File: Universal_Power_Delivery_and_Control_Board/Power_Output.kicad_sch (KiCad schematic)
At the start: 40 parts, among them CN1 B03B-XASK-1-A(LF)(SN), CN2 B03B-XASK-1-A(LF)(SN), CN3 B03B-XASK-1-A(LF)(SN), CN4 B03B-XASK-1-A(LF)(SN), U10 SN74LVC1G17DCKR, U11 SN74LVC1G17DCKR, U12 SN74LVC1G17DCKR, U13 SN74LVC1G17DCKR, U14 SN74LVC1G17DCKR, U8 TPS51385RJNR, U9 TPS24751RUVR

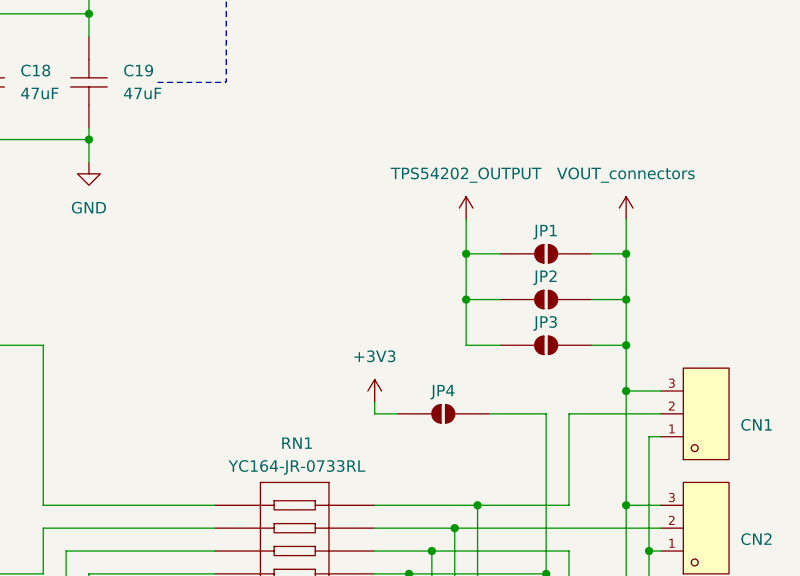
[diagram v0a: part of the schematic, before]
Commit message: Switched to a 4 layer stackup and routed the digital output section.
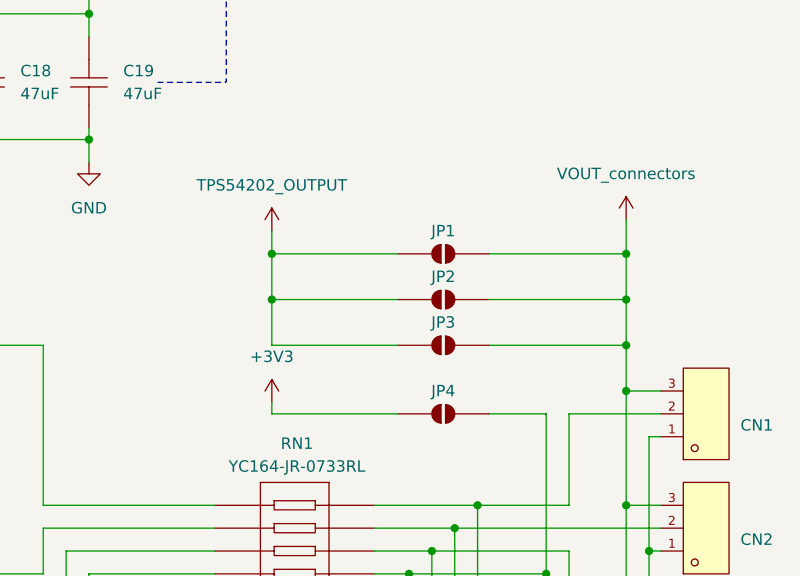
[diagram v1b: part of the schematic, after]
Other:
- moved on the sheet: JP1, JP2, JP3
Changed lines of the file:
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@@
 	)
 	(junction
-		(at 227.33 69.85)
-		(diameter 0)
-		(color 0 0 0 0)
-	)
-	(junction
 		(at 247.65 142.24)
 		(diameter 0)
@@
 	)
 	(junction
+		(at 245.11 64.77)
+		(diameter 0)
+		(color 0 0 0 0)
+	)
+	(junction
+		(at 245.11 69.85)
+		(diameter 0)
+		(color 0 0 0 0)
+	)
+	(junction
 		(at 245.11 80.01)
 		(diameter 0)
@@
 	)
 	(junction
-		(at 227.33 64.77)
-		(diameter 0)
-		(color 0 0 0 0)
-	)
-	(junction
 		(at 223.52 97.79)
 		(diameter 0)
@@
 	)
 	(junction
+		(at 205.74 69.85)
+		(diameter 0)
+		(color 0 0 0 0)
+	)
+	(junction
 		(at 137.16 38.1)
 		(diameter 0)
@@
 	)
 	(junction
-		(at 245.11 64.77)
+		(at 205.74 64.77)
 		(diameter 0)
 		(color 0 0 0 0)
@@
 	)
 	(junction
-		(at 245.11 69.85)
-		(diameter 0)
-		(color 0 0 0 0)
-	)
-	(junction
 		(at 146.05 176.53)
 		(diameter 0)
@@
 	(wire
 		(pts
-			(xy 217.17 81.28) (xy 217.17 82.55)
+			(xy 205.74 81.28) (xy 205.74 82.55)
 		)
 		(stroke
@@
 	(wire
 		(pts
-			(xy 227.33 60.96) (xy 227.33 64.77)
+			(xy 205.74 62.23) (xy 205.74 64.77)
 		)
 		(stroke
@@
 	(wire
 		(pts
-			(xy 227.33 69.85) (xy 227.33 74.93)
+			(xy 205.74 69.85) (xy 205.74 74.93)
 		)
 		(stroke
@@
 	(wire
 		(pts
+			(xy 205.74 69.85) (xy 219.71 69.85)
+		)
+		(stroke
+			(width 0)
+			(type default)
+		)
+	)
+	(wire
+		(pts
 			(xy 78.74 104.14) (xy 97.79 104.14)
 		)
@@
 	(wire
 		(pts
-			(xy 245.11 64.77) (xy 245.11 74.93)
+			(xy 245.11 64.77) (xy 245.11 69.85)
 		)
 		(stroke
@@
 	(wire
 		(pts
-			(xy 227.33 64.77) (xy 231.14 64.77)
-		)
-		(stroke
-			(width 0)
-			(type default)
-		)
-	)
-	(wire
-		(pts
 			(xy 76.2 156.21) (xy 76.2 158.75)
 		)
@@
 	(wire
 		(pts
-			(xy 227.33 64.77) (xy 227.33 69.85)
+			(xy 205.74 64.77) (xy 205.74 69.85)
 		)
 		(stroke
@@
 	(wire
 		(pts
-			(xy 241.3 74.93) (xy 245.11 74.93)
+			(xy 229.87 74.93) (xy 245.11 74.93)
 		)
 		(stroke
@@
 	(wire
 		(pts
-			(xy 217.17 82.55) (xy 219.71 82.55)
+			(xy 205.74 82.55) (xy 219.71 82.55)
 		)
 		(stroke
@@
 	(wire
 		(pts
-			(xy 241.3 64.77) (xy 245.11 64.77)
+			(xy 229.87 64.77) (xy 245.11 64.77)
 		)
 		(stroke
@@
 	(wire
 		(pts
+			(xy 205.74 64.77) (xy 219.71 64.77)
+		)
+		(stroke
+			(width 0)
+			(type default)
+		)
+	)
+	(wire
+		(pts
 			(xy 247.65 123.19) (xy 248.92 123.19)
 		)
@@
 	(wire
 		(pts
-			(xy 241.3 69.85) (xy 245.11 69.85)
+			(xy 229.87 69.85) (xy 245.11 69.85)
 		)
 		(stroke
@@
 	(wire
 		(pts
-			(xy 227.33 69.85) (xy 231.14 69.85)
-		)
-		(stroke
-			(width 0)
-			(type default)
-		)
-	)
-	(wire
-		(pts
 			(xy 146.05 144.78) (xy 146.05 151.13)
 		)
@@
 	(wire
 		(pts
-			(xy 227.33 74.93) (xy 231.14 74.93)
+			(xy 205.74 74.93) (xy 219.71 74.93)
 		)
 		(stroke
@@
 	(wire
 		(pts
+			(xy 245.11 69.85) (xy 245.11 74.93)
+		)
+		(stroke
+			(width 0)
+			(type default)
+		)
+	)
+	(wire
+		(pts
 			(xy 116.84 140.97) (xy 116.84 138.43)
 		)
@@
 	(symbol
 		(lib_id "power:+1V0")
-		(at 217.17 81.28 0)
+		(at 205.74 81.28 0)
 		(unit 1)
 		(body_style 1)
@@
 		(fields_autoplaced yes)
 		(property "Reference" "#PWR043"
-			(at 217.17 85.09 0)
+			(at 205.74 85.09 0)
 			(hide yes)
 			(show_name no)
@@
 		)
 		(property "Value" "+3V3"
-			(at 217.17 76.2 0)
+			(at 205.74 76.2 0)
 			(show_name no)
 			(do_not_autoplace no)
@@
 		)
 		(property "Footprint" ""
-			(at 217.17 81.28 0)
+			(at 205.74 81.28 0)
 			(hide yes)
 			(show_name no)
@@
 		)
 		(property "Datasheet" ""
-			(at 217.17 81.28 0)
+			(at 205.74 81.28 0)
 			(hide yes)
 			(show_name no)
@@
 		)
 		(property "Description" "Power symbol creates a global label with name \"+1V0\""
-			(at 217.17 81.28 0)
+			(at 205.74 81.28 0)
 			(hide yes)
 			(show_name no)
@@
 	(symbol
 		(lib_id "Jumper:SolderJumper_2_Open")
-		(at 236.22 69.85 0)
+		(at 224.79 69.85 0)
 		(unit 1)
 		(body_style 1)
@@
 		(dnp no)
 		(property "Reference" "JP2"
-			(at 236.22 67.31 0)
+			(at 224.79 67.31 0)
 			(show_name no)
 			(do_not_autoplace no)
@@
 		)
 		(property "Value" "SolderJumper_2_Open"
-			(at 236.22 66.04 0)
+			(at 224.79 66.04 0)
 			(hide yes)
 			(show_name no)
@@
 		)
 		(property "Footprint" "Jumper:SolderJumper-2_P1.3mm_Open_RoundedPad1.0x1.5mm"
-			(at 236.22 69.85 0)
+			(at 224.79 69.85 0)
 			(hide yes)
 			(show_name no)
@@
 		)
 		(property "Datasheet" ""
-			(at 236.22 77.47 0)
+			(at 224.79 77.47 0)
 			(hide yes)
 			(show_name no)
@@
 		)
 		(property "Description" "Solder Jumper, 2-pole, open"
-			(at 236.22 74.93 0)
+			(at 224.79 74.93 0)
 			(hide yes)
 			(show_name no)
@@
 	(symbol
 		(lib_id "Jumper:SolderJumper_2_Open")
-		(at 236.22 64.77 0)
+		(at 224.79 64.77 0)
 		(unit 1)
 		(body_style 1)
@@
 		(dnp no)
 		(property "Reference" "JP1"
-			(at 236.22 62.23 0)
+			(at 224.79 62.23 0)
 			(show_name no)
 			(do_not_autoplace no)
@@
 		)
 		(property "Value" "SolderJumper_2_Open"
-			(at 236.22 60.96 0)
+			(at 224.79 60.96 0)
 			(hide yes)
 			(show_name no)
@@
 		)
 		(property "Footprint" "Jumper:SolderJumper-2_P1.3mm_Open_RoundedPad1.0x1.5mm"
-			(at 236.22 64.77 0)
+			(at 224.79 64.77 0)
 			(hide yes)
 			(show_name no)
@@
 		)
 		(property "Datasheet" ""
-			(at 236.22 72.39 0)
+			(at 224.79 72.39 0)
 			(hide yes)
 			(show_name no)
@@
 		)
 		(property "Description" "Solder Jumper, 2-pole, open"
-			(at 236.22 69.85 0)
+			(at 224.79 69.85 0)
 			(hide yes)
 			(show_name no)
@@
 	(symbol
 		(lib_id "power:+1V0")
-		(at 227.33 60.96 0)
+		(at 205.74 62.23 0)
 		(unit 1)
 		(body_style 1)
@@
 		(fields_autoplaced yes)
 		(property "Reference" "#PWR041"
-			(at 227.33 64.77 0)
+			(at 205.74 66.04 0)
 			(hide yes)
 			(show_name no)
@@
 		)
 		(property "Value" "TPS54202_OUTPUT"
-			(at 227.33 55.88 0)
+			(at 205.74 57.15 0)
 			(show_name no)
 			(do_not_autoplace no)
@@
 		)
 		(property "Footprint" ""
-			(at 227.33 60.96 0)
+			(at 205.74 62.23 0)
 			(hide yes)
 			(show_name no)
@@
 		)
 		(property "Datasheet" ""
-			(at 227.33 60.96 0)
+			(at 205.74 62.23 0)
 			(hide yes)
 			(show_name no)
@@
 		)
 		(property "Description" "Power symbol creates a global label with name \"+1V0\""
-			(at 227.33 60.96 0)
+			(at 205.74 62.23 0)
 			(hide yes)
 			(show_name no)
@@
 	(symbol
 		(lib_id "Jumper:SolderJumper_2_Open")
-		(at 236.22 74.93 0)
+		(at 224.79 74.93 0)
 		(unit 1)
 		(body_style 1)
@@
 		(dnp no)
 		(property "Reference" "JP3"
-			(at 236.22 72.39 0)
+			(at 224.79 72.39 0)
 			(show_name no)
 			(do_not_autoplace no)
@@
 		)
 		(property "Value" "SolderJumper_2_Open"
-			(at 236.22 71.12 0)
+			(at 224.79 71.12 0)
 			(hide yes)
 			(show_name no)
@@
 		)
 		(property "Footprint" "Jumper:SolderJumper-2_P1.3mm_Open_RoundedPad1.0x1.5mm"
-			(at 236.22 74.93 0)
+			(at 224.79 74.93 0)
 			(hide yes)
 			(show_name no)
@@
 		)
 		(property "Datasheet" ""
-			(at 236.22 82.55 0)
+			(at 224.79 82.55 0)
 			(hide yes)
 			(show_name no)
@@
 		)
 		(property "Description" "Solder Jumper, 2-pole, open"
-			(at 236.22 80.01 0)
+			(at 224.79 80.01 0)
 			(hide yes)
 			(show_name no)

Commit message: Practically finshed the digital output layout, added the i2c io expander as im short on ios.
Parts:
- added C41: 10uF, Capacitor_SMD:C_0805_2012Metric_Pad1.18x1.45mm_HandSolder, symbol Device:C
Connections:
- net +5V_VSYS: now also C41.2
- net GND: now also C41.1
- net at CN1.2, RN1.8: now also FPC1.3; no longer FPC1.1
- net at CN4.2, JP4.2 (B), RN1.5: now also FPC1.9; no longer FPC1.7
- net at CN2.2, RN1.7: now also FPC1.5; no longer FPC1.3
- net at CN3.2, RN1.6: now also FPC1.7; no longer FPC1.5
- net at R18.1: now also FPC1.1; no longer FPC1.9
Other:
- moved on the sheet: R18

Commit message: Added some misc stuff layout almost finished.
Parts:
- removed JP3: SolderJumper_2_Open, Jumper:SolderJumper-2_P1.3mm_Open_RoundedPad1.0x1.5mm, symbol Jumper:SolderJumper_2_Open
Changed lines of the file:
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@@
 	)
 	(junction
-		(at 245.11 74.93)
-		(diameter 0)
-		(color 0 0 0 0)
-	)
-	(junction
 		(at 76.2 153.67)
 		(diameter 0)
@@
 	)
 	(junction
-		(at 205.74 69.85)
-		(diameter 0)
-		(color 0 0 0 0)
-	)
-	(junction
 		(at 137.16 38.1)
 		(diameter 0)
@@
 	(wire
 		(pts
-			(xy 245.11 74.93) (xy 245.11 80.01)
+			(xy 245.11 69.85) (xy 245.11 80.01)
 		)
 		(stroke
@@
 	(wire
 		(pts
-			(xy 205.74 69.85) (xy 205.74 74.93)
-		)
-		(stroke
-			(width 0)
-			(type default)
-		)
-	)
-	(wire
-		(pts
 			(xy 96.52 73.66) (xy 91.44 73.66)
 		)
@@
 	(wire
 		(pts
-			(xy 229.87 74.93) (xy 245.11 74.93)
-		)
-		(stroke
-			(width 0)
-			(type default)
-		)
-	)
-	(wire
-		(pts
 			(xy 223.52 149.86) (xy 248.92 149.86)
 		)
@@
 	(wire
 		(pts
-			(xy 205.74 74.93) (xy 219.71 74.93)
-		)
-		(stroke
-			(width 0)
-			(type default)
-		)
-	)
-	(wire
-		(pts
 			(xy 228.6 139.7) (xy 228.6 92.71)
 		)
@@
 	(wire
 		(pts
-			(xy 245.11 69.85) (xy 245.11 74.93)
-		)
-		(stroke
-			(width 0)
-			(type default)
-		)
-	)
-	(wire
-		(pts
 			(xy 116.84 140.97) (xy 116.84 138.43)
 		)
@@
 					(unit 1)
 				)
-			)
-		)
-	)
-	(symbol
-		(lib_id "Jumper:SolderJumper_2_Open")
-		(at 224.79 74.93 0)
-		(unit 1)
-		(body_style 1)
-		(exclude_from_sim no)
-		(in_bom no)
-		(on_board yes)
-		(in_pos_files yes)
-		(dnp no)
-		(property "Reference" "JP3"
-			(at 224.79 72.39 0)
-			(show_name no)
-			(do_not_autoplace no)
-			(effects
-				(font
-					(size 1.27 1.27)
-				)
-			)
-		)
-		(property "Value" "SolderJumper_2_Open"
-			(at 224.79 71.12 0)
-			(hide yes)
-			(show_name no)
-			(do_not_autoplace no)
-			(effects
-				(font
-					(size 1.27 1.27)
-				)
-			)
-		)
-		(property "Footprint" "Jumper:SolderJumper-2_P1.3mm_Open_RoundedPad1.0x1.5mm"
-			(at 224.79 74.93 0)
-			(hide yes)
-			(show_name no)
-			(do_not_autoplace no)
-			(effects
-				(font
-					(size 1.27 1.27)
-				)
-			)
-		)
-		(property "Datasheet" ""
-			(at 224.79 82.55 0)
-			(hide yes)
-			(show_name no)
-			(do_not_autoplace no)
-			(effects
-				(font
-					(size 1.27 1.27)
-				)
-			)
-		)
-		(property "Description" "Solder Jumper, 2-pole, open"
-			(at 224.79 80.01 0)
-			(hide yes)
-			(show_name no)
-			(do_not_autoplace no)
-			(effects
-				(font
-					(size 1.27 1.27)
-				)
-			)
-		)
-		(pin "1"
-		)
-		(pin "2"
-		)
-		(instances
-			(project "Universal_Power_Delivery_and_Control_Board"
-				(path "/b749dd2f-6b66-411b-a989-65da6091f700/a6d714a7-b982-4119-8ec1-595454fba1af"
-					(reference "JP3")
-					(unit 1)
-				)

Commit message: Practically finished layout, need to route the buttons.
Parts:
- added JP11, JP3: SolderJumper_2_Open, Jumper:SolderJumper-2_P1.3mm_Open_RoundedPad1.0x1.5mm, symbol Jumper:SolderJumper_2_Open
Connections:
- net +5V_VSYS: now also JP3.2 (B); no longer C28.1, C29.1, C30.1, C31.1, C32.1, C41.2, U10.5 (VCC), U11.5 (VCC), U12.5 (VCC), U13.5 (VCC), U14.5 (VCC)
- net GND: now also C41.2; no longer C41.1
- net VOUT_connectors: now also JP11.2 (B)
- new net: C28.1, C29.1, C30.1, C31.1, C32.1, C41.1, JP11.1 (A), JP3.1 (A), U10.5 (VCC), U11.5 (VCC), U12.5 (VCC), U13.5 (VCC), U14.5 (VCC)
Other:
- moved on the sheet: C41, JP1, JP2, JP4

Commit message: Fished layout for now, need to add some components for optional functionality.
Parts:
- added R47: 10K, Resistor_SMD:R_0402_1005Metric_Pad0.72x0.64mm_HandSolder, symbol Device:R
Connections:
- net +3V3: now also R47.1
- net PG_TPS51385: now also R47.2
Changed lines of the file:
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@@
 	)
 	(junction
+		(at 92.71 55.88)
+		(diameter 0)
+		(color 0 0 0 0)
+	)
+	(junction
 		(at 228.6 92.71)
 		(diameter 0)
@@
 	(wire
 		(pts
+			(xy 92.71 55.88) (xy 97.79 55.88)
+		)
+		(stroke
+			(width 0)
+			(type default)
+		)
+	)
+	(wire
+		(pts
 			(xy 245.11 118.11) (xy 248.92 118.11)
 		)
@@
 	(wire
 		(pts
+			(xy 92.71 22.86) (xy 92.71 25.4)
+		)
+		(stroke
+			(width 0)
+			(type default)
+		)
+	)
+	(wire
+		(pts
 			(xy 146.05 74.93) (xy 146.05 93.98)
 		)
@@
 	(wire
 		(pts
-			(xy 90.17 55.88) (xy 97.79 55.88)
+			(xy 90.17 55.88) (xy 92.71 55.88)
 		)
 		(stroke
@@
 	(wire
 		(pts
+			(xy 92.71 33.02) (xy 92.71 55.88)
+		)
+		(stroke
+			(width 0)
+			(type default)
+		)
+	)
+	(wire
+		(pts
 			(xy 236.22 120.65) (xy 248.92 120.65)
 		)
@@
 	)
 	(symbol
+		(lib_id "power:+1V0")
+		(at 92.71 22.86 0)
+		(unit 1)
+		(body_style 1)
+		(exclude_from_sim no)
+		(in_bom yes)
+		(on_board yes)
+		(in_pos_files yes)
+		(dnp no)
+		(fields_autoplaced yes)
+		(property "Reference" "#PWR095"
+			(at 92.71 26.67 0)
+			(hide yes)
+			(show_name no)
+			(do_not_autoplace no)
+			(effects
+				(font
+					(size 1.27 1.27)
+				)
+			)
+		)
+		(property "Value" "+3V3"
+			(at 92.71 17.78 0)
+			(show_name no)
+			(do_not_autoplace no)
+			(effects
+				(font
+					(size 1.27 1.27)
+				)
+			)
+		)
+		(property "Footprint" ""
+			(at 92.71 22.86 0)
+			(hide yes)
+			(show_name no)
+			(do_not_autoplace no)
+			(effects
+				(font
+					(size 1.27 1.27)
+				)
+			)
+		)
+		(property "Datasheet" ""
+			(at 92.71 22.86 0)
+			(hide yes)
+			(show_name no)
+			(do_not_autoplace no)
+			(effects
+				(font
+					(size 1.27 1.27)
+				)
+			)
+		)
+		(property "Description" "Power symbol creates a global label with name \"+1V0\""
+			(at 92.71 22.86 0)
+			(hide yes)
+			(show_name no)
+			(do_not_autoplace no)
+			(effects
+				(font
+					(size 1.27 1.27)
+				)
+			)
+		)
+		(pin "1"
+		)
+		(instances
+			(project "Universal_Power_Delivery_and_Control_Board"
+				(path "/b749dd2f-6b66-411b-a989-65da6091f700/a6d714a7-b982-4119-8ec1-595454fba1af"
+					(reference "#PWR095")
+					(unit 1)
+				)
+			)
+		)
+	)
+	(symbol
 		(lib_id "Device:R")
 		(at 58.42 165.1 0)
@@
 					(unit 1)
 				)
+			)
+		)
+	)
+	(symbol
+		(lib_id "Device:R")
+		(at 92.71 29.21 0)
+		(unit 1)
+		(body_style 1)
+		(exclude_from_sim no)
+		(in_bom yes)
+		(on_board yes)
+		(in_pos_files yes)
+		(dnp no)
+		(property "Reference" "R47"
+			(at 95.25 27.9399 0)
+			(show_name no)
+			(do_not_autoplace no)
+			(effects
+				(font
+					(size 1.27 1.27)
+				)
+				(justify left)
+			)
+		)
+		(property "Value" "10K"
+			(at 95.25 30.4799 0)
+			(show_name no)
+			(do_not_autoplace no)
+			(effects
+				(font
+					(size 1.27 1.27)
+				)
+				(justify left)
+			)
+		)
+		(property "Footprint" "Resistor_SMD:R_0402_1005Metric_Pad0.72x0.64mm_HandSolder"
+			(at 90.932 29.21 90)
+			(hide yes)
+			(show_name no)
+			(do_not_autoplace no)
+			(effects
+				(font
+					(size 1.27 1.27)
+				)
+			)
+		)
+		(property "Datasheet" ""
+			(at 92.71 29.21 0)
+			(hide yes)
+			(show_name no)
+			(do_not_autoplace no)
+			(effects
+				(font
+					(size 1.27 1.27)
+				)
+			)
+		)
+		(property "Description" "Resistor"
+			(at 92.71 29.21 0)
+			(hide yes)
+			(show_name no)
+			(do_not_autoplace no)
+			(effects
+				(font
+					(size 1.27 1.27)
+				)
+			)
+		)
+		(pin "1"
+		)
+		(pin "2"
+		)
+		(instances
+			(project "Universal_Power_Delivery_and_Control_Board"
+				(path "/b749dd2f-6b66-411b-a989-65da6091f700/a6d714a7-b982-4119-8ec1-595454fba1af"
+					(reference "R47")
+					(unit 1)
+				)

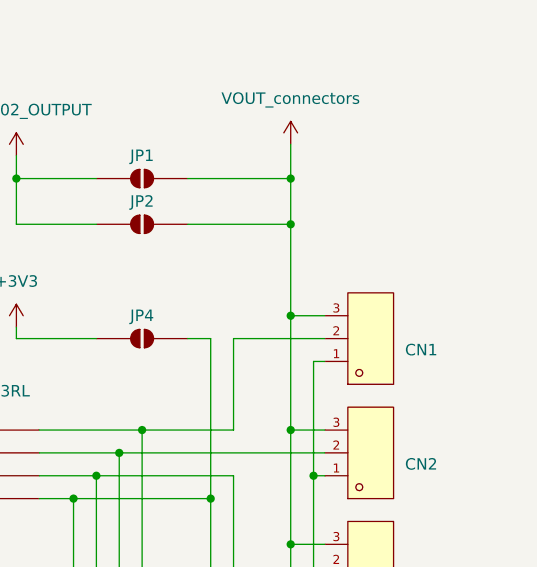
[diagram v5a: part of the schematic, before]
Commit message: Finished layout 0 DRC errors.
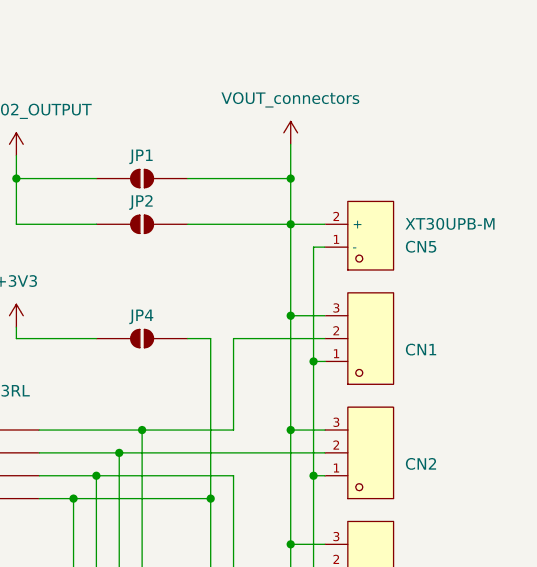
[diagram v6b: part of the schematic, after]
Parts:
- added CN5: XT30UPB-M, lcsc_footprints:C428721_CONN-TH_XT30UPB-M, symbol lcsc_imported:XT30UPB-M
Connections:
- net GND: now also CN5.1 (-)
- net VOUT_connectors: now also CN5.2 (+)
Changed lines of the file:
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@@
 	)
 	(junction
+		(at 247.65 85.09)
+		(diameter 0)
+		(color 0 0 0 0)
+	)
+	(junction
 		(at 226.06 95.25)
 		(diameter 0)
@@
 	(wire
 		(pts
+			(xy 245.11 69.85) (xy 248.92 69.85)
+		)
+		(stroke
+			(width 0)
+			(type default)
+		)
+	)
+	(wire
+		(pts
 			(xy 214.63 64.77) (xy 214.63 69.85)
 		)
@@
 	(wire
 		(pts
+			(xy 247.65 72.39) (xy 247.65 85.09)
+		)
+		(stroke
+			(width 0)
+			(type default)
+		)
+	)
+	(wire
+		(pts
 			(xy 153.67 144.78) (xy 146.05 144.78)
 		)
@@
 	(wire
 		(pts
+			(xy 248.92 72.39) (xy 247.65 72.39)
+		)
+		(stroke
+			(width 0)
+			(type default)
+		)
+	)
+	(wire
+		(pts
 			(xy 220.98 154.94) (xy 248.92 154.94)
 		)
@@
 					(unit 1)
 				)
+			)
+		)
+	)
+	(symbol
+		(lib_id "lcsc_imported:XT30UPB-M")
+		(at 254 71.12 0)
+		(mirror x)
+		(unit 1)
+		(body_style 1)
+		(exclude_from_sim no)
+		(in_bom yes)
+		(on_board yes)
+		(in_pos_files yes)
+		(dnp no)
+		(property "Reference" "CN5"
+			(at 257.81 72.3901 0)
+			(show_name no)
+			(do_not_autoplace no)
+			(effects
+				(font
+					(size 1.27 1.27)
+				)
+				(justify left)
+			)
+		)
+		(property "Value" "XT30UPB-M"
+			(at 257.81 69.8501 0)
+			(show_name no)
+			(do_not_autoplace no)
+			(effects
+				(font
+					(size 1.27 1.27)
+				)
+				(justify left)
+			)
+		)
+		(property "Footprint" "lcsc_footprints:C428721_CONN-TH_XT30UPB-M"
+			(at 254 60.96 0)
+			(hide yes)
+			(show_name no)
+			(do_not_autoplace no)
+			(effects
+				(font
+					(size 1.27 1.27)
+				)
+			)
+		)
+		(property "Datasheet" "https://www.lcsc.com/datasheet/lcsc_datasheet_2304241822_Changzhou-Amass-Elec-XT30UPB-M_C428721.pdf"
+			(at 251.714 71.247 0)
+			(hide yes)
+			(show_name no)
+			(do_not_autoplace no)
+			(effects
+				(font
+					(size 1.27 1.27)
+				)
+			)
+		)
+		(property "Description" "XT30UPB-M"
+			(at 254 71.12 0)
+			(hide yes)
+			(show_name no)
+			(do_not_autoplace no)
+			(effects
+				(font
+					(size 1.27 1.27)
+				)
+			)
+		)
+		(property "LCSC" "C428721"
+			(at 254 71.12 0)
+			(hide yes)
+			(show_name no)
+			(do_not_autoplace no)
+			(effects
+				(font
+					(size 1.27 1.27)
+				)
+			)
+		)
+		(property "Manufacturer" "AMASS(艾迈斯)"
+			(at 254 71.12 0)
+			(hide yes)
+			(show_name no)
+			(do_not_autoplace no)
+			(effects
+				(font
+					(size 1.27 1.27)
+				)
+			)
+		)
+		(pin "2"
+		)
+		(pin "1"
+		)
+		(instances
+			(project "Universal_Power_Delivery_and_Control_Board"
+				(path "/b749dd2f-6b66-411b-a989-65da6091f700/a6d714a7-b982-4119-8ec1-595454fba1af"
+					(reference "CN5")
+					(unit 1)
+				)
